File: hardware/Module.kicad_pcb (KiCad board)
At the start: 2 copper layers, 57.5 x 109.2 mm, 27 parts, among them J1 CV_OUT, J11 RIGHT, J2 CV2, J3 CV1, J4 CV3, J5 CV_TRIGGER, J8 CV4, J9 LEFT, SW5 BUTTON_1, SW6 BUTTON_6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

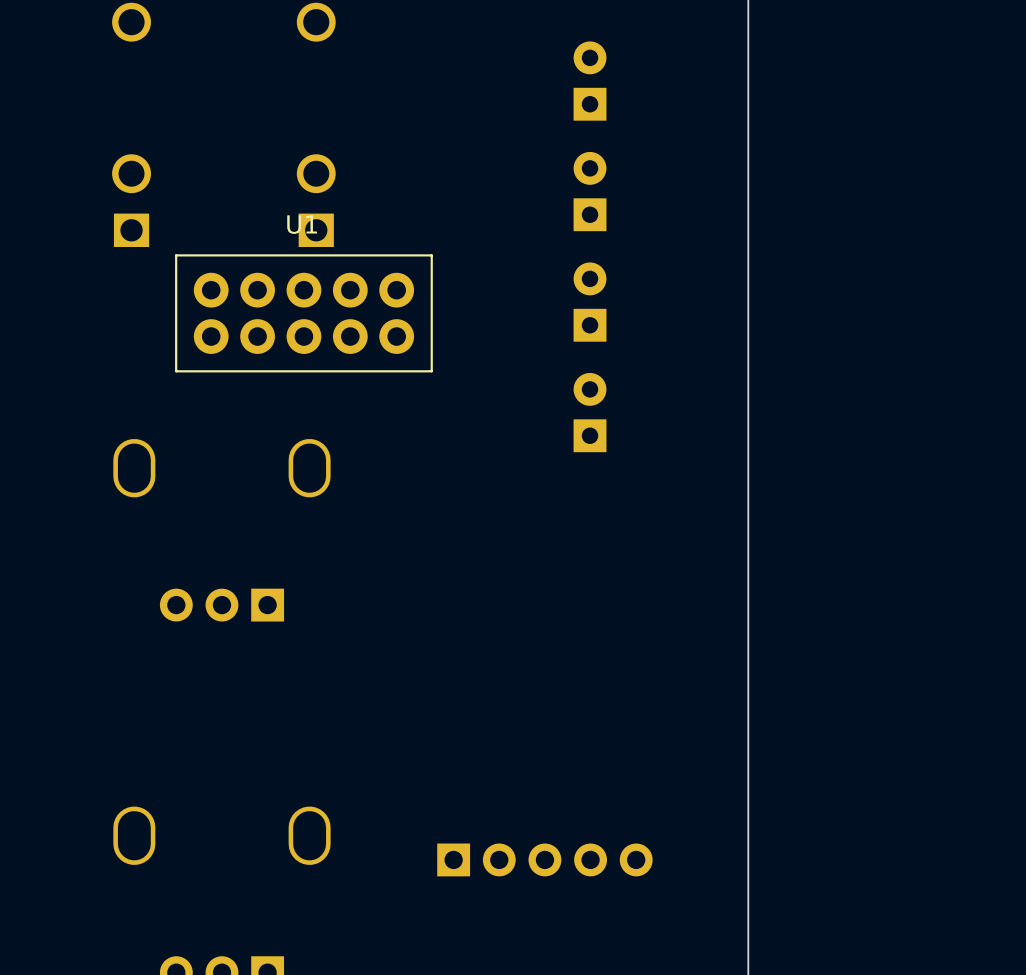
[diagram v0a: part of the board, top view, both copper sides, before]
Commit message: Patch a rough schematic
Signed-off-by: Petr Horacek <petr@zlosynth.com>
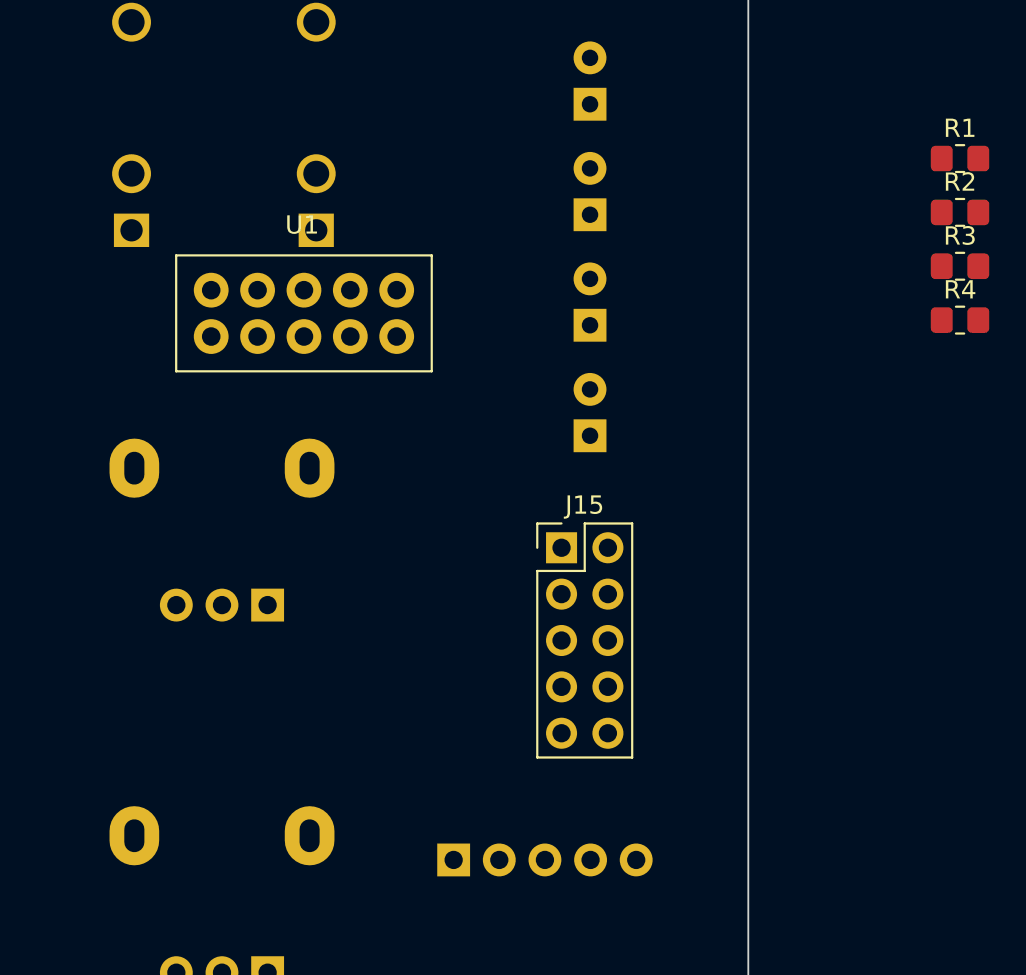
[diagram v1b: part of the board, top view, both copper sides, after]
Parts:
- added J15: POWER, Connector_PinHeader_2.54mm:PinHeader_2x05_P2.54mm_Vertical, F.Cu at (96.2, 101.7)
- added R1: 1k, Resistor_SMD:R_0805_2012Metric_Pad1.20x1.40mm_HandSolder, F.Cu at (118.0, 80.4)
- added R2: 1k, Resistor_SMD:R_0805_2012Metric_Pad1.20x1.40mm_HandSolder, F.Cu at (118.0, 83.3)
- added R3: 1k, Resistor_SMD:R_0805_2012Metric_Pad1.20x1.40mm_HandSolder, F.Cu at (118.0, 86.3)
- added R4: 1k, Resistor_SMD:R_0805_2012Metric_Pad1.20x1.40mm_HandSolder, F.Cu at (118.0, 89.2)
- D1: renamed from D7; value LED7 -> LED1
- D2: renamed from D5; value LED5 -> LED2
- D4: renamed from D1; value LED1 -> LED4
- J1: renamed from J5; value CV_TRIGGER -> CV_IN_1
- J10: renamed from J1; value CV_OUT -> GATE_OUT_2
- J11: renamed from J8; value CV4 -> AUDIO_IN_L
- J12: renamed from J9; value LEFT -> AUDIO_IN_R
- J13: renamed from J11; value RIGHT -> AUDIO_OUT_L
- J14: renamed from J11; value RIGHT -> AUDIO_OUT_R
- J2: renamed from J5; value CV_TRIGGER -> CV_IN_2
- J3: renamed from J4; value CV3 -> CV_IN_3
- J4: renamed from J3; value CV1 -> CV_IN_4
- J5: renamed from J2; value CV2 -> CV_OUT_1
- J6: renamed from J1; value CV_OUT -> CV_OUT_2
- J7: renamed from J4; value CV3 -> GATE_IN_1
- J8: renamed from J3; value CV1 -> GATE_IN_2
- J9: renamed from J2; value CV2 -> GATE_OUT_1
- RV1: renamed from RV7; footprint Custom:Potentiometer_Thonk_Trimmer -> Potentiometer_THT:Potentiometer_Alpha_RD901F-40-00D_Single_Vertical
- RV3: renamed from RV6; footprint Custom:Potentiometer_Thonk_Trimmer -> Potentiometer_THT:Potentiometer_Alpha_RD901F-40-00D_Single_Vertical
- SW1: renamed from SW7; value SW_Rotary_1x8_MP -> ROTARY_SWITCH
- SW3: renamed from SW6; value BUTTON_6 -> BUTTON_2
- renumbered RV3 to RV2, SW5 to SW2
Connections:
- net CV_5 renamed CV_IN_5
- J1 pad T: CV_TRIGGER -> CV_IN_1
- J1 pad TN: unconnected-(J5-PadTN) -> unconnected-(J1-PadTN)
- J10 pad T: CV_OUT -> GATE_OUT_2
- J10 pad TN: unconnected-(J1-PadTN) -> unconnected-(J10-PadTN)
- J11 pad T: CV_4 -> LEFT_IN
- J11 pad TN: Net-(J8-PadTN) -> unconnected-(J11-PadTN)
- J12 pad T: unconnected-(J9-PadT) -> RIGHT_IN
- J13 pad T: unconnected-(J11-PadT) -> LEFT_OUT
- J13 pad TN: unconnected-(J11-PadTN) -> unconnected-(J13-PadTN)
- J14 pad T: unconnected-(J11-PadT) -> RIGHT_OUT
- J14 pad TN: unconnected-(J11-PadTN) -> unconnected-(J14-PadTN)
- J2 pad T: CV_TRIGGER -> CV_2
- J2 pad TN: unconnected-(J5-PadTN) -> unconnected-(J2-PadTN)
- J3 pad TN: Net-(J4-PadTN) -> unconnected-(J3-PadTN)
- J4 pad T: CV_1 -> CV_4
- J4 pad TN: Net-(J3-PadTN) -> unconnected-(J4-PadTN)
- J5 pad T: CV_2 -> CV_OUT_1
- J5 pad TN: Net-(J2-PadTN) -> unconnected-(J5-PadTN)
- J6 pad T: CV_OUT -> CV_OUT_2
- J6 pad TN: unconnected-(J1-PadTN) -> unconnected-(J6-PadTN)
- J7 pad T: CV_3 -> GATE_IN_1
- J7 pad TN: Net-(J4-PadTN) -> unconnected-(J7-PadTN)
- J8 pad T: CV_1 -> GATE_IN_2
- J8 pad TN: Net-(J3-PadTN) -> unconnected-(J8-PadTN)
- J9 pad T: CV_2 -> GATE_OUT_1
- J9 pad TN: Net-(J2-PadTN) -> unconnected-(J9-PadTN)
- RV1 pad 2: POT_6 -> POT_1
- RV1 pad 3: +3.3V -> +5V
- RV2 pad 2: POT_5 -> POT_2
- RV2 pad 3: +3.3V -> +5V
- RV3 pad 2: POT_3 -> POT_5
- SW1 pad 1: unconnected-(SW7-Pad1) -> GND
- SW1 pad 2: unconnected-(SW7-Pad2) -> SWITCH_1
- SW1 pad 3: unconnected-(SW7-Pad3) -> SWITCH_2
- SW1 pad 4: unconnected-(SW7-Pad4) -> SWITCH_3
- SW1 pad 5: unconnected-(SW7-Pad5) -> SWITCH_4
- SW1 pad 6: unconnected-(SW7-Pad6) -> SWITCH_5
- SW1 pad 7: unconnected-(SW7-Pad7) -> SWITCH_6
- SW1 pad 8: unconnected-(SW7-Pad8) -> SWITCH_7
- SW1 pad 9: unconnected-(SW7-Pad9) -> SWITCH_8
- SW3 pad 2: BUTTON_6 -> BUTTON_2
- U1 pad A2: POT_3 -> SWITCH_3
- U1 pad A3: POT_1 -> SWITCH_4
- U1 pad A8: BUTTON_3 -> SWITCH_6
- U1 pad A9: BUTTON_4 -> SWITCH_5
- U1 pad B10: CV_RSNX -> GATE_IN_1
- U1 pad B3: unconnected-(U1-AUDIO_IN_R-PadB3) -> RIGHT_IN
- U1 pad B4: unconnected-(U1-AUDIO_IN_L-PadB4) -> LEFT_IN
- U1 pad B5: PROBE -> GATE_OUT_1
- U1 pad B6: unconnected-(U1-GATE_OUT_2-PadB6) -> GATE_OUT_2
- U1 pad B9: CV_TRIGGER -> GATE_IN_2
- U1 pad C1: unconnected-(U1-CV_OUT_2-PadC1) -> CV_OUT_2
- U1 pad C10: CV_OUT -> CV_OUT_1
- U1 pad C2: POT_6 -> POT_1
- U1 pad C3: POT_5 -> POT_2
- U1 pad C4: POT_7 -> POT_3
- U1 pad C5: CV_3 -> POT_4
- U1 pad C6: CV_4 -> CV_IN_4
- U1 pad C8: CV_2 -> CV_IN_2
- U1 pad C9: CV_1 -> CV_IN_1
- U1 pad D1: LED_SER -> SWITCH_7
- U1 pad D2: LED_SRCLK -> SWITCH_2
- U1 pad D3: LED_RCLK -> SWITCH_1
- U1 pad D4: unconnected-(U1-SDMMC_D1-PadD4) -> LED_4
- U1 pad D5: BUTTON_6 -> LED_3
- U1 pad D6: BUTTON_5 -> LED_1
- U1 pad D7: unconnected-(U1-SDMMC_CMD-PadD7) -> LED_2
- U1 pad D8: POT_4 -> unconnected-(U1-SPI_MISO-PadD8)
- U1 pad D9: POT_2 -> SWITCH_8

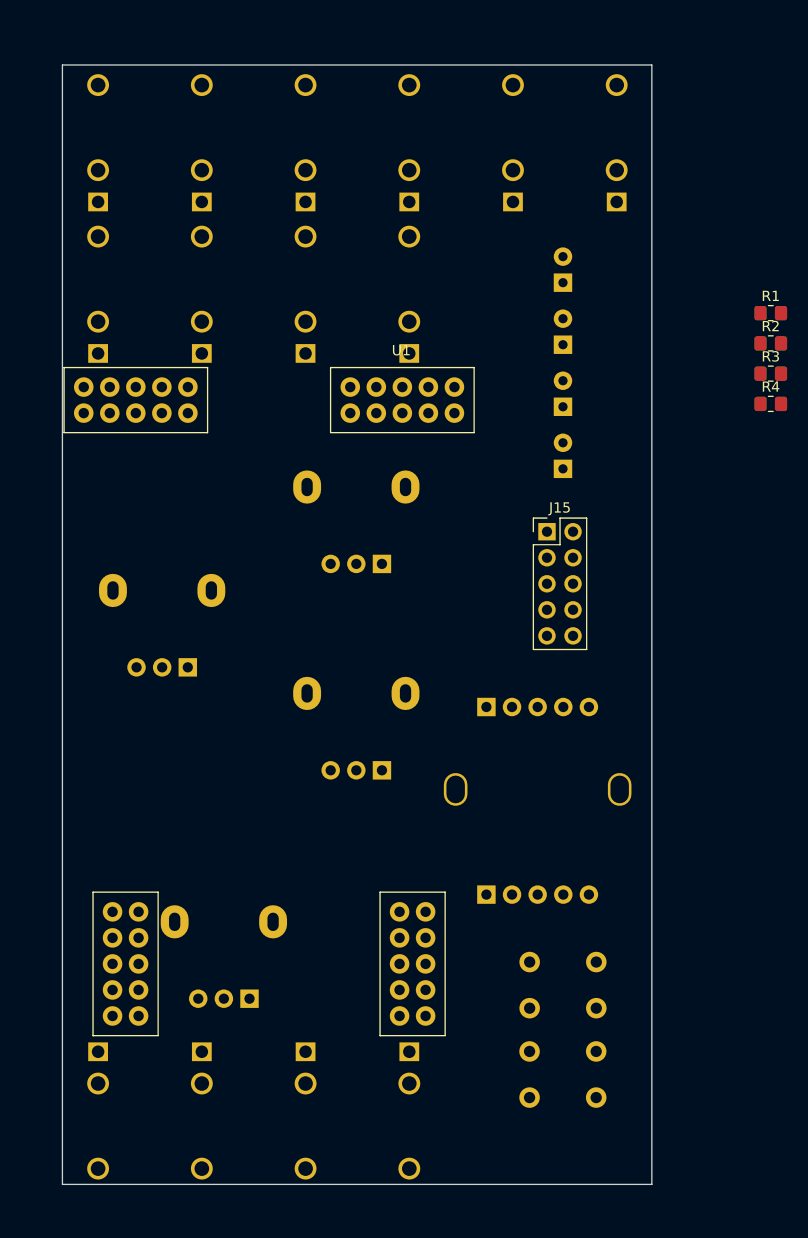
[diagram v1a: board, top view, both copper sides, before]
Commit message: First wire up of the PCB
Signed-off-by: Petr Horacek <petr@zlosynth.com>
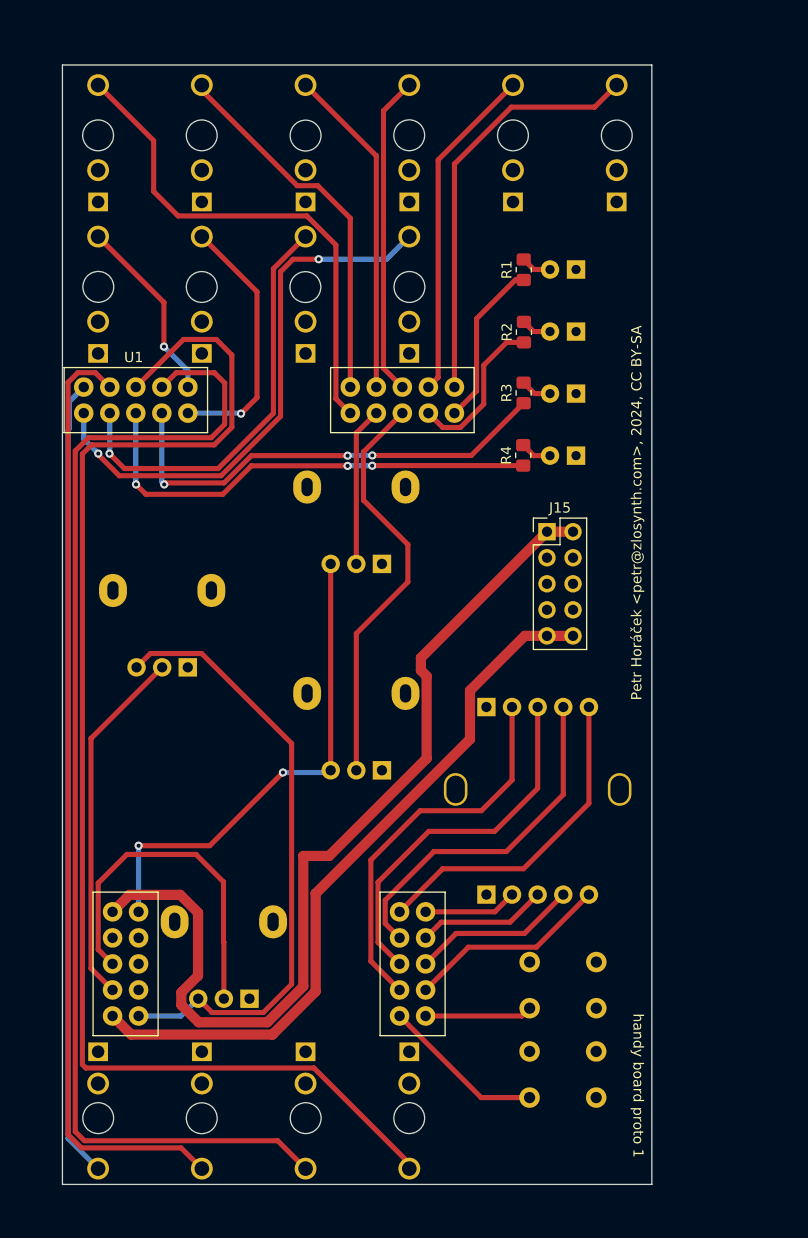
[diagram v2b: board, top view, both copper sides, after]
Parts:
- moved R4 24.7 mm to (93.8, 94.2), turned to 90 degrees
- moved R1 24.5 mm to (93.9, 76.1), turned to 90 degrees
- moved R3 24.2 mm to (93.9, 88.1), turned to 90 degrees
- moved R2 24.1 mm to (93.9, 82.2), turned to 90 degrees
- moved D1 1.81 mm to (99.0, 76.1), turned to 180 degrees
- moved D2 1.81 mm to (99.0, 82.2), turned to 180 degrees
- moved D3 1.81 mm to (99.0, 88.2), turned to 180 degrees
- moved D4 1.81 mm to (99.0, 94.3), turned to 180 degrees
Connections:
- J2 pad T: CV_2 -> CV_IN_2
- J3 pad T: CV_3 -> CV_IN_3
- J4 pad T: CV_4 -> CV_IN_4
- RV2 pad 3: +5V -> +3.3V
- RV3 pad 2: POT_5 -> POT_3
- RV3 pad 3: +3.3V -> +5V
- U1 pad A2: SWITCH_3 -> POT_2
- U1 pad A3: SWITCH_4 -> POT_4
- U1 pad A8: SWITCH_6 -> unconnected-(U1-USB_DM-PadA8)
- U1 pad A9: SWITCH_5 -> unconnected-(U1-USB_DP-PadA9)
- U1 pad B3: RIGHT_IN -> LEFT_IN
- U1 pad B4: LEFT_IN -> RIGHT_IN
- U1 pad B5: GATE_OUT_1 -> GATE_OUT_2
- U1 pad B6: GATE_OUT_2 -> GATE_OUT_1
- U1 pad B7: BUTTON_1 -> LED_3
- U1 pad B8: BUTTON_2 -> LED_4
- U1 pad C1: CV_OUT_2 -> CV_OUT_1
- U1 pad C10: CV_OUT_1 -> CV_OUT_2
- U1 pad C2: POT_1 -> CV_IN_4
- U1 pad C3: POT_2 -> CV_IN_3
- U1 pad C4: POT_3 -> CV_IN_2
- U1 pad C5: POT_4 -> CV_IN_1
- U1 pad C6: CV_IN_4 -> LED_1
- U1 pad C7: CV_IN_5 -> LED_2
- U1 pad C8: CV_IN_2 -> POT_3
- U1 pad C9: CV_IN_1 -> POT_1
- U1 pad D1: SWITCH_7 -> BUTTON_2
- U1 pad D10: unconnected-(U1-SPI_SCK-PadD10) -> BUTTON_1
- U1 pad D2: SWITCH_2 -> SWITCH_8
- U1 pad D3: SWITCH_1 -> SWITCH_7
- U1 pad D4: LED_4 -> SWITCH_6
- U1 pad D5: LED_3 -> SWITCH_5
- U1 pad D6: LED_1 -> SWITCH_1
- U1 pad D7: LED_2 -> SWITCH_2
- U1 pad D8: unconnected-(U1-SPI_MISO-PadD8) -> SWITCH_3
- U1 pad D9: SWITCH_8 -> SWITCH_4
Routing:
- net LEFT_IN: track 0.00 -> 130.6 mm
- net RIGHT_IN: track 0.00 -> 117.2 mm
- net LEFT_OUT: track 0.00 -> 92.8 mm
- net VCC: track 0.00 -> 92.1 mm
- net RIGHT_OUT: track 0.00 -> 78.1 mm
- net VEE: track 0.00 -> 70.2 mm
- net +3.3V: track 0.00 -> 60.1 mm
- net GATE_IN_1: track 0.00 -> 53.8 mm, vias 0 -> 2
- net CV_OUT_2: track 0.00 -> 49.5 mm
- net +5V: track 0.00 -> 48.4 mm, vias 0 -> 2
- net LED_4: track 0.00 -> 46.3 mm, vias 0 -> 3
- net LED_3: track 0.00 -> 45.4 mm, vias 0 -> 3
- net GATE_IN_2: track 0.00 -> 41.3 mm, vias 0 -> 1
- net CV_IN_1: track 0.00 -> 40.8 mm
- net POT_3: track 0.00 -> 40.3 mm
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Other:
- outline, holes or cut-outs redrawn
- board text added: "Petr Horáček <petr@zlosynth.com>, 2024, CC BY-SA"
- board text added: "handy board proto 1"

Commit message: Complete the ground plane and fix ERC
Signed-off-by: Petr Horacek <petr@zlosynth.com>
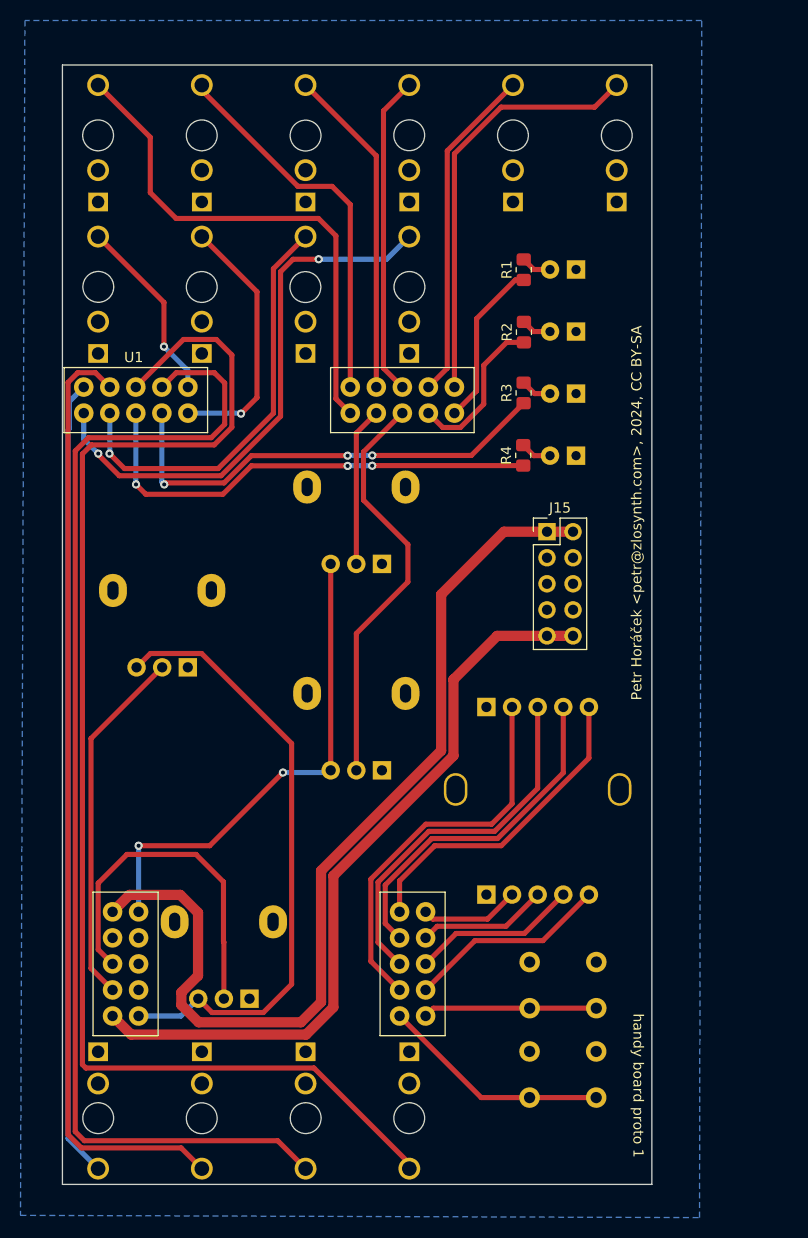
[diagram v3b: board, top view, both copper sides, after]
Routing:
- net BUTTON_2: track 16.0 -> 22.5 mm
- net BUTTON_1: track 10.5 -> 17.0 mm
- net VEE: track 70.2 -> 73.6 mm
- net VCC: track 92.1 -> 94.6 mm
- net SWITCH_5: track 32.3 -> 31.4 mm
- net CV_OUT_1: track 36.6 -> 37.4 mm
- net CV_OUT_2: track 49.5 -> 50.3 mm
- net SWITCH_1: track 9.13 -> 9.71 mm
- net CV_IN_1: track 40.8 -> 41.4 mm
- added copper zone on B.Cu, net GND
